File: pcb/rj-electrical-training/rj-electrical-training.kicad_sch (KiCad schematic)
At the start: 0 parts

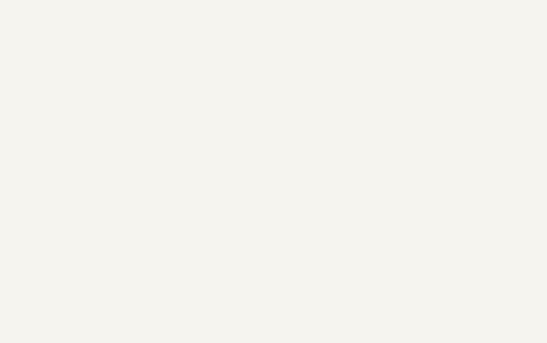
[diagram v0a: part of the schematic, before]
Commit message: Added I2C sensors and components
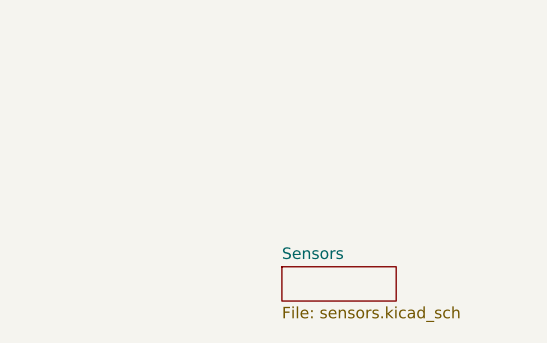
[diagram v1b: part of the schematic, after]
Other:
- added sheet Sensors (sensors.kicad_sch)
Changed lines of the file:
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@@
+	)
+	(sheet
+		(at 280.67 146.05)
+		(size 12.7 3.81)
+		(exclude_from_sim no)
+		(in_bom yes)
+		(on_board yes)
+		(dnp no)
+		(fields_autoplaced yes)
+		(stroke
+			(width 0.1524)
+			(type solid)
+		)
+		(fill
+			(color 0 0 0 0)
+		)
+		(property "Sheetname" "Sensors"
+			(at 280.67 145.3384 0)
+			(show_name no)
+			(do_not_autoplace no)
+			(effects
+				(font
+					(size 1.27 1.27)
+				)
+				(justify left bottom)
+			)
+		)
+		(property "Sheetfile" "sensors.kicad_sch"
+			(at 280.67 150.4446 0)
+			(show_name no)
+			(do_not_autoplace no)
+			(effects
+				(font
+					(size 1.27 1.27)
+				)
+				(justify left top)
+			)
+		)
+		(instances
+			(project "rj-electrical-training"
+				(path "/5fd6e245-9295-49fb-811c-6efb339b53e4"
+					(page "8")
+				)
+			)
+		)
 	)
 	(sheet

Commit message: Integrated LEDs to circuit
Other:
- sheet Indicator LEDs ports: added color_sensor_led, slave_power_led, usb_power_led; removed ind_led[0..6]
- sheet MCU ports: added slave_power_led; removed ind_led[0..6]
- sheet Sensors ports: added color_sensor_led; removed none
- sheet USB & Debug Connectors ports: added usb_power_led; removed none
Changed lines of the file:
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@@
+	(bus
+		(pts
+			(xy 109.22 135.89) (xy 158.75 135.89)
+		)
+		(stroke
+			(width 0)
+			(type default)
+		)
+	)
+	(bus
+		(pts
+			(xy 162.56 124.46) (xy 165.1 124.46)
+		)
+		(stroke
+			(width 0)
+			(type default)
+		)
+	)
 	(bus
 		(pts
@@
 	(bus
 		(pts
-			(xy 152.4 120.65) (xy 165.1 120.65)
+			(xy 107.95 152.4) (xy 162.56 152.4)
+		)
+		(stroke
+			(width 0)
+			(type default)
+		)
+	)
+	(bus
+		(pts
+			(xy 158.75 121.92) (xy 165.1 121.92)
+		)
+		(stroke
+			(width 0)
+			(type default)
+		)
+	)
+	(bus
+		(pts
+			(xy 101.6 100.33) (xy 109.22 100.33)
+		)
+		(stroke
+			(width 0)
+			(type default)
+		)
+	)
+	(bus
+		(pts
+			(xy 152.4 119.38) (xy 165.1 119.38)
+		)
+		(stroke
+			(width 0)
+			(type default)
+		)
+	)
+	(bus
+		(pts
+			(xy 109.22 100.33) (xy 109.22 135.89)
+		)
+		(stroke
+			(width 0)
+			(type default)
+		)
+	)
+	(bus
+		(pts
+			(xy 158.75 135.89) (xy 158.75 121.92)
+		)
+		(stroke
+			(width 0)
+			(type default)
+		)
+	)
+	(bus
+		(pts
+			(xy 162.56 124.46) (xy 162.56 152.4)
 		)
 		(stroke
@@
 			)
 		)
-		(pin "ind_led[0..6]" output
-			(at 152.4 120.65 0)
+		(pin "slave_power_led" output
+			(at 152.4 119.38 0)
 			(effects
 				(font
@@
 	)
 	(sheet
-		(at 280.67 146.05)
-		(size 12.7 3.81)
+		(at 71.12 146.05)
+		(size 36.83 17.78)
 		(exclude_from_sim no)
 		(in_bom yes)
@@
 		)
 		(property "Sheetname" "Sensors"
-			(at 280.67 145.3384 0)
+			(at 71.12 145.3384 0)
 			(show_name no)
 			(do_not_autoplace no)
@@
 		)
 		(property "Sheetfile" "sensors.kicad_sch"
-			(at 280.67 150.4446 0)
+			(at 71.12 164.4146 0)
 			(show_name no)
 			(do_not_autoplace no)
@@
 				)
 				(justify left top)
+			)
+		)
+		(pin "color_sensor_led" output
+			(at 107.95 152.4 0)
+			(effects
+				(font
+					(size 1.27 1.27)
+				)
+				(justify right)
 			)
 		)
@@
 			)
 		)
+		(pin "usb_power_led" output
+			(at 101.6 100.33 0)
+			(effects
+				(font
+					(size 1.27 1.27)
+				)
+				(justify right)
+			)
+		)
 		(instances
 			(project "rj-electrical-training"
@@
 			)
 		)
-		(pin "ind_led[0..6]" input
-			(at 165.1 120.65 180)
-			(effects
-				(font
+		(pin "slave_power_led" input
+			(at 165.1 119.38 180)
+			(effects
+				(font
+					(size 1.27 1.27)
+				)
+				(justify left)
+			)
+		)
+		(pin "usb_power_led" input
+			(at 165.1 121.92 180)
+			(effects
+				(font
+					(size 1.27 1.27)
+				)
+				(justify left)
+			)
+		)
+		(pin "color_sensor_led" input
+			(at 165.1 124.46 180)
+			(effects
+				(font
